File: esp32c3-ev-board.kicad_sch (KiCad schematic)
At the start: 23 parts, among them IC1 ESP32-C3, IC3 ACS711EEXTK-31AB-T, J1 Battery Neg(Series), J2 Battery Pos

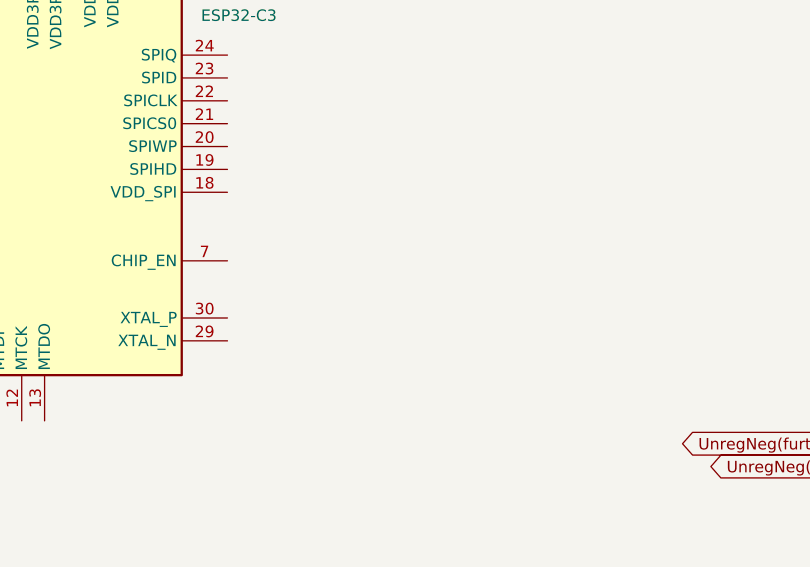
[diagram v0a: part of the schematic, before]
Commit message: Crystal added
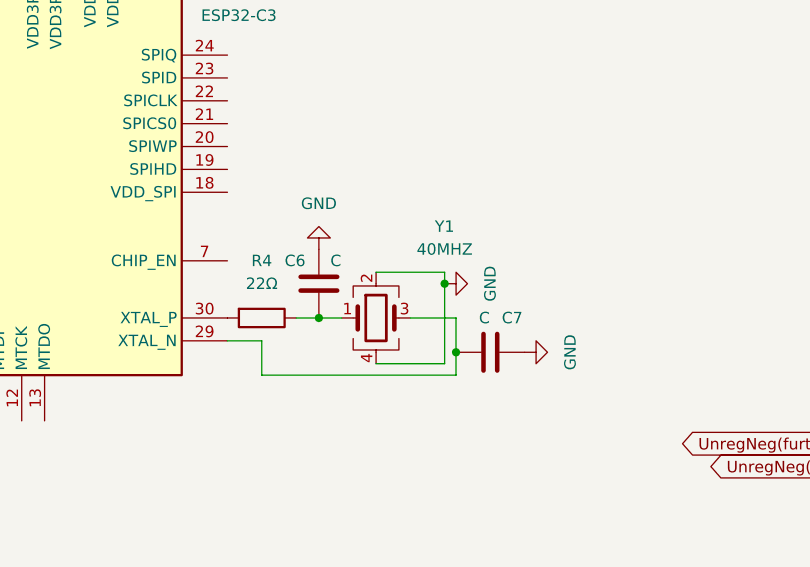
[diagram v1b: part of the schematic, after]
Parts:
- added C6, C7: C, symbol Device:C
- added R4: 22Ω, symbol Device:R
- added Y1: 40MHZ, symbol Device:Crystal_GND24
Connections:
- net GND: now also C6.2, C7.2, Y1.2, Y1.4
- net at IC1.29 (XTAL_N): now also C7.1, Y1.3
- net at IC1.30 (XTAL_P): now also R4.2
- new net: C6.1, R4.1, Y1.1
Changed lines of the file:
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@@
   (junction (at 33.02 69.85) (diameter 0) (color 0 0 0 0)
   )
+  (junction (at 116.84 101.6) (diameter 0) (color 0 0 0 0)
+  )
   (junction (at 77.47 54.61) (diameter 0) (color 0 0 0 0)
   )
@@
   )
   (junction (at 116.84 45.72) (diameter 0) (color 0 0 0 0)
+  )
+  (junction (at 130.81 97.79) (diameter 0) (color 0 0 0 0)
+  )
+  (junction (at 132.08 105.41) (diameter 0) (color 0 0 0 0)
   )
   (junction (at 60.96 29.21) (diameter 0) (color 0 0 0 0)
@@
     (stroke (width 0) (type default))
   )
+  (wire (pts (xy 132.08 105.41) (xy 132.08 107.95))
+    (stroke (width 0) (type default))
+  )
+  (wire (pts (xy 110.49 104.14) (xy 106.68 104.14))
+    (stroke (width 0) (type default))
+  )
   (wire (pts (xy 91.44 38.1) (xy 91.44 54.61))
     (stroke (width 0) (type default))
@@
     (stroke (width 0) (type default))
   )
+  (wire (pts (xy 132.08 101.6) (xy 132.08 105.41))
+    (stroke (width 0) (type default))
+  )
+  (wire (pts (xy 130.81 106.68) (xy 123.19 106.68))
+    (stroke (width 0) (type default))
+  )
+  (wire (pts (xy 130.81 97.79) (xy 130.81 106.68))
+    (stroke (width 0) (type default))
+  )
   (wire (pts (xy 103.505 38.1) (xy 97.155 38.1))
     (stroke (width 0) (type default))
@@
     (stroke (width 0) (type default))
   )
+  (wire (pts (xy 116.84 101.6) (xy 114.3 101.6))
+    (stroke (width 0) (type default))
+  )
   (wire (pts (xy 201.93 95.25) (xy 201.93 100.33))
     (stroke (width 0) (type default))
@@
     (stroke (width 0) (type default))
   )
+  (wire (pts (xy 127 101.6) (xy 132.08 101.6))
+    (stroke (width 0) (type default))
+  )
+  (wire (pts (xy 119.38 101.6) (xy 116.84 101.6))
+    (stroke (width 0) (type default))
+  )
   (wire (pts (xy 29.21 73.66) (xy 29.21 77.47))
     (stroke (width 0) (type default))
@@
     (stroke (width 0) (type default))
   )
+  (wire (pts (xy 123.19 96.52) (xy 130.81 96.52))
+    (stroke (width 0) (type default))
+  )
   (wire (pts (xy 189.23 132.08) (xy 189.23 135.89))
     (stroke (width 0) (type default))
@@
     (stroke (width 0) (type default))
   )
+  (wire (pts (xy 110.49 107.95) (xy 110.49 104.14))
+    (stroke (width 0) (type default))
+  )
+  (wire (pts (xy 130.81 96.52) (xy 130.81 97.79))
+    (stroke (width 0) (type default))
+  )
   (wire (pts (xy 48.26 69.85) (xy 60.96 69.85))
+    (stroke (width 0) (type default))
+  )
+  (wire (pts (xy 132.08 107.95) (xy 110.49 107.95))
     (stroke (width 0) (type default))
   )
@@
     )
   )
+  (symbol (lib_id "Device:Crystal_GND24") (at 123.19 101.6 0) (unit 1)
+    (in_bom yes) (on_board yes) (dnp no)
+    (property "Reference" "Y1" (at 130.81 91.44 0)
+      (effects (font (size 1.27 1.27)))
+    )
+    (property "Value" "40MHZ" (at 130.81 93.98 0)
+      (effects (font (size 1.27 1.27)))
+    )
+    (property "Footprint" "" (at 123.19 101.6 0)
+      (effects (font (size 1.27 1.27)) hide)
+    )
+    (property "Datasheet" "~" (at 123.19 101.6 0)
+      (effects (font (size 1.27 1.27)) hide)
+    )
+    (pin "1")
+    (pin "2")
+    (pin "3")
+    (pin "4")
+    (instances
+      (project "esp32c3-ev-board"
+        (path "/f5da1fcc-93b5-4c63-bb34-c18c11bc243c"
+          (reference "Y1") (unit 1)
+        )
+      )
+    )
+  )
   (symbol (lib_id "Device:D") (at 189.23 139.7 90) (unit 1)
     (in_bom yes) (on_board yes) (dnp no) (fields_autoplaced)
@@
         (path "/f5da1fcc-93b5-4c63-bb34-c18c11bc243c"
           (reference "#PWR04") (unit 1)
+        )
+      )
+    )
+  )
+  (symbol (lib_id "power:GND") (at 139.7 105.41 90) (unit 1)
+    (in_bom yes) (on_board yes) (dnp no) (fields_autoplaced)
+    (property "Reference" "#PWR09" (at 146.05 105.41 0)
+      (effects (font (size 1.27 1.27)) hide)
+    )
+    (property "Value" "GND" (at 144.78 105.41 0)
+      (effects (font (size 1.27 1.27)))
+    )
+    (property "Footprint" "" (at 139.7 105.41 0)
+      (effects (font (size 1.27 1.27)) hide)
+    )
+    (property "Datasheet" "" (at 139.7 105.41 0)
+      (effects (font (size 1.27 1.27)) hide)
+    )
+    (pin "1")
+    (instances
+      (project "esp32c3-ev-board"
+        (path "/f5da1fcc-93b5-4c63-bb34-c18c11bc243c"
+          (reference "#PWR09") (unit 1)
         )
       )
@@
     )
   )
+  (symbol (lib_id "Device:C") (at 135.89 105.41 90) (unit 1)
+    (in_bom yes) (on_board yes) (dnp no)
+    (property "Reference" "C7" (at 137.16 101.6 90)
+      (effects (font (size 1.27 1.27)) (justify right))
+    )
+    (property "Value" "C" (at 134.62 101.6 90)
+      (effects (font (size 1.27 1.27)) (justify right))
+    )
+    (property "Footprint" "" (at 139.7 104.4448 0)
+      (effects (font (size 1.27 1.27)) hide)
+    )
+    (property "Datasheet" "~" (at 135.89 105.41 0)
+      (effects (font (size 1.27 1.27)) hide)
+    )
+    (pin "1")
+    (pin "2")
+    (instances
+      (project "esp32c3-ev-board"
+        (path "/f5da1fcc-93b5-4c63-bb34-c18c11bc243c"
+          (reference "C7") (unit 1)
+        )
+      )
+    )
+  )
   (symbol (lib_id "Connector:Screw_Terminal_01x01") (at 137.16 182.88 270) (unit 1)
     (in_bom yes) (on_board yes) (dnp no)
@@
     )
   )
+  (symbol (lib_id "Device:C") (at 116.84 97.79 180) (unit 1)
+    (in_bom yes) (on_board yes) (dnp no)
+    (property "Reference" "C6" (at 113.03 95.25 0)
+      (effects (font (size 1.27 1.27)) (justify right))
+    )
+    (property "Value" "C" (at 118.11 95.25 0)
+      (effects (font (size 1.27 1.27)) (justify right))
+    )
+    (property "Footprint" "" (at 115.8748 93.98 0)
+      (effects (font (size 1.27 1.27)) hide)
+    )
+    (property "Datasheet" "~" (at 116.84 97.79 0)
+      (effects (font (size 1.27 1.27)) hide)
+    )
+    (pin "1")
+    (pin "2")
+    (instances
+      (project "esp32c3-ev-board"
+        (path "/f5da1fcc-93b5-4c63-bb34-c18c11bc243c"
+          (reference "C6") (unit 1)
+        )
+      )
+    )
+  )
+  (symbol (lib_id "power:GND") (at 116.84 93.98 180) (unit 1)
+    (in_bom yes) (on_board yes) (dnp no) (fields_autoplaced)
+    (property "Reference" "#PWR08" (at 116.84 87.63 0)
+      (effects (font (size 1.27 1.27)) hide)
+    )
+    (property "Value" "GND" (at 116.84 88.9 0)
+      (effects (font (size 1.27 1.27)))
+    )
+    (property "Footprint" "" (at 116.84 93.98 0)
+      (effects (font (size 1.27 1.27)) hide)
+    )
+    (property "Datasheet" "" (at 116.84 93.98 0)
+      (effects (font (size 1.27 1.27)) hide)
+    )
+    (pin "1")
+    (instances
+      (project "esp32c3-ev-board"
+        (path "/f5da1fcc-93b5-4c63-bb34-c18c11bc243c"
+          (reference "#PWR08") (unit 1)
+        )
+      )
+    )
+  )
   (symbol (lib_id "Device:C") (at 193.04 135.89 90) (unit 1)
     (in_bom yes) (on_board yes) (dnp no)
@@
         )
       )
+    )
+  )
+  (symbol (lib_id "Device:R") (at 110.49 101.6 270) (unit 1)
+    (in_bom yes) (on_board yes) (dnp no) (fields_autoplaced)
+    (property "Reference" "R4" (at 110.49 95.25 90)
+      (effects (font (size 1.27 1.27)))
+    )
+    (property "Value" "22Ω" (at 110.49 97.79 90)
+      (effects (font (size 1.27 1.27)))
+    )
+    (property "Footprint" "" (at 110.49 99.822 90)
+      (effects (font (size 1.27 1.27)) hide)
+    )
+    (property "Datasheet" "~" (at 110.49 101.6 0)
+      (effects (font (size 1.27 1.27)) hide)
+    )
+    (pin "1")
+    (pin "2")
+    (instances
+      (project "esp32c3-ev-board"
+        (path "/f5da1fcc-93b5-4c63-bb34-c18c11bc243c"
+          (reference "R4") (unit 1)
+        )
+      )
+    )
+  )
+  (symbol (lib_id "power:GND") (at 130.81 97.79 90) (unit 1)
+    (in_bom yes) (on_board yes) (dnp no) (fields_autoplaced)
+    (property "Reference" "#PWR010" (at 137.16 97.79 0)
+      (effects (font (size 1.27 1.27)) hide)
+    )
+    (property "Value" "GND" (at 135.89 97.79 0)
+      (effects (font (size 1.27 1.27)))
+    )
+    (property "Footprint" "" (at 130.81 97.79 0)
+      (effects (font (size 1.27 1.27)) hide)
+    )
+    (property "Datasheet" "" (at 130.81 97.79 0)
+      (effects (font (size 1.27 1.27)) hide)
+    )
+    (pin "1")
+    (instances
+      (project "esp32c3-ev-board"
+        (path "/f5da1fcc-93b5-4c63-bb34-c18c11bc243c"
+          (reference "#PWR010") (unit 1)
+        )
+      )

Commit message: rando resistor test
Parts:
- added R5: 22Ω, symbol Device:R
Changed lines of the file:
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@@
+    )
+  )
+  (symbol (lib_id "Device:R") (at 132.08 83.82 270) (unit 1)
+    (in_bom yes) (on_board yes) (dnp no) (fields_autoplaced)
+    (property "Reference" "R5" (at 132.08 77.47 90)
+      (effects (font (size 1.27 1.27)))
+    )
+    (property "Value" "22Ω" (at 132.08 80.01 90)
+      (effects (font (size 1.27 1.27)))
+    )
+    (property "Footprint" "" (at 132.08 82.042 90)
+      (effects (font (size 1.27 1.27)) hide)
+    )
+    (property "Datasheet" "~" (at 132.08 83.82 0)
+      (effects (font (size 1.27 1.27)) hide)
+    )
+    (pin "1")
+    (pin "2")
+    (instances
+      (project "esp32c3-ev-board"
+        (path "/f5da1fcc-93b5-4c63-bb34-c18c11bc243c"
+          (reference "R5") (unit 1)
+        )
+      )
     )
   )

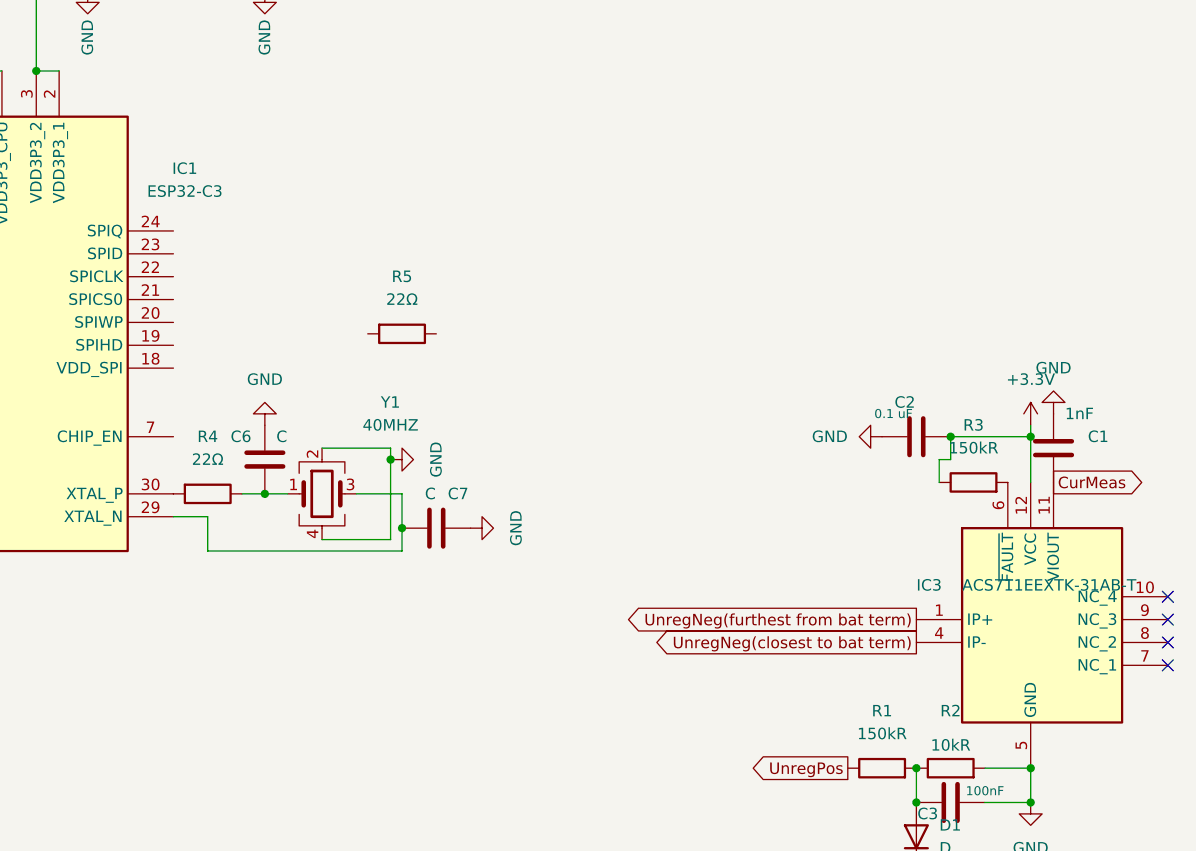
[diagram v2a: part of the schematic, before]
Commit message: Flash Memory Added
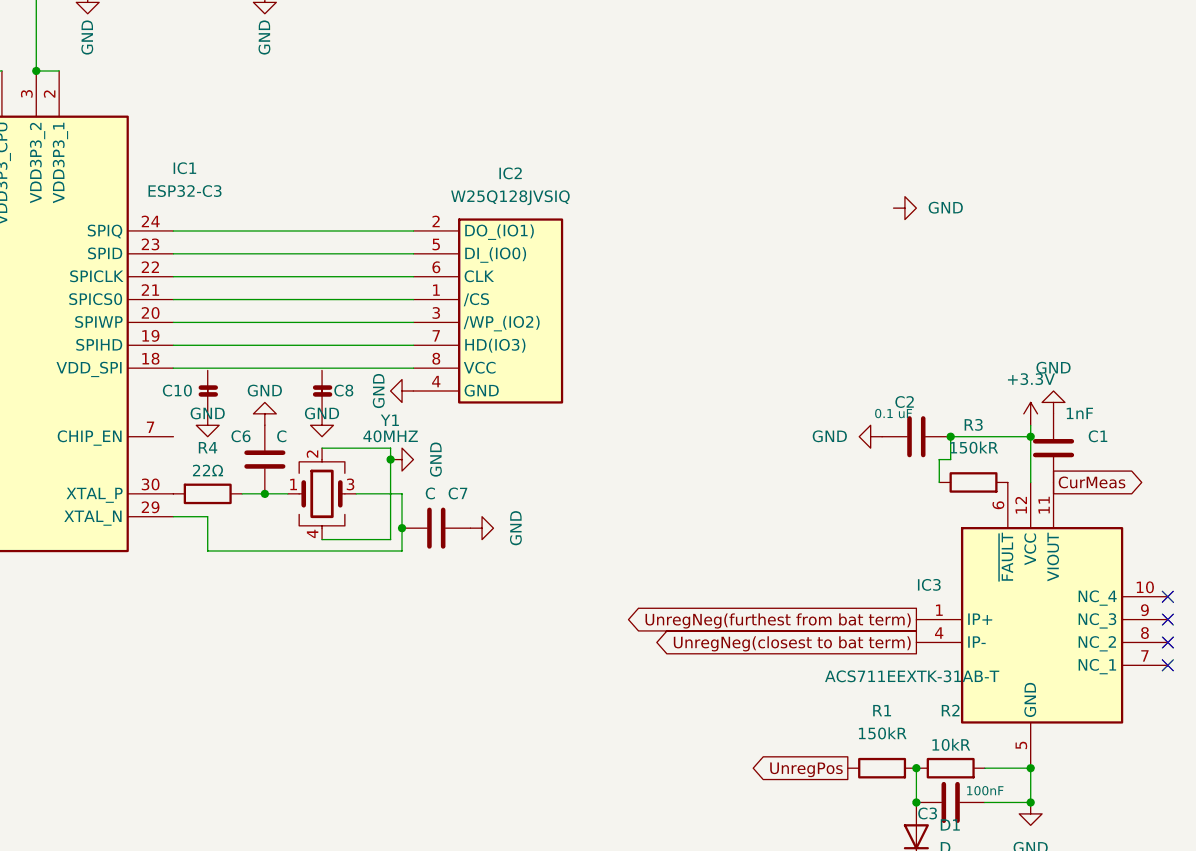
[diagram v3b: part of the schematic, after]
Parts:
- removed R5: 22Ω, symbol Device:R
- added C10, C8: C, symbol Device:C
- added IC2: W25Q128JVSIQ, SOIC127P790X216-8N, symbol W25Q128JVSIQ:W25Q128JVSIQ
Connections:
- net GND: now also C10.2, C8.2, IC2.4 (GND)
- net at IC1.18 (VDD_SPI): now also IC2.8 (VCC)
- net at IC1.19 (SPIHD): now also IC2.7 (HD(IO3))
- net at IC1.20 (SPIWP): now also IC2.3 (/WP_(IO2))
- net at IC1.21 (SPICS0): now also IC2.1 (/CS)
- net at IC1.22 (SPICLK): now also IC2.6 (CLK)
- net at IC1.23 (SPID): now also IC2.5 (DI_(IO0))
- net at IC1.24 (SPIQ): now also IC2.2 (DO_(IO1))

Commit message: Cleaning up Schematic
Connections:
- net at IC1.18 (VDD_SPI), IC2.8 (VCC): now also C10.1, C8.1

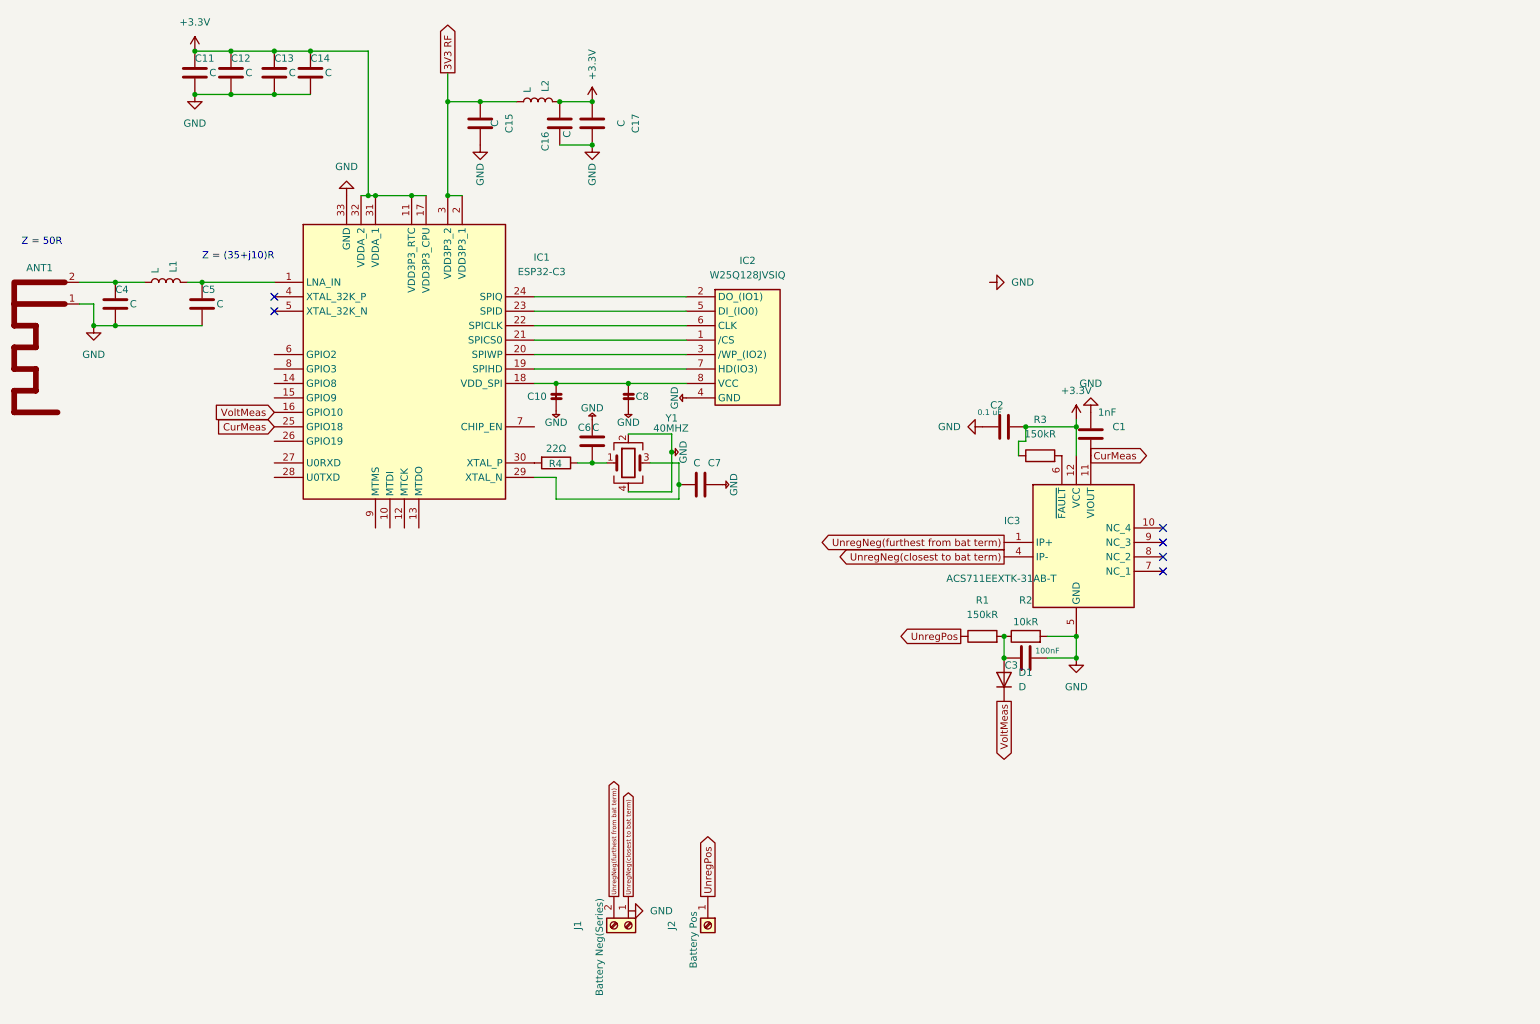
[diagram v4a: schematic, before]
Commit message: Added Chip Enable Switch
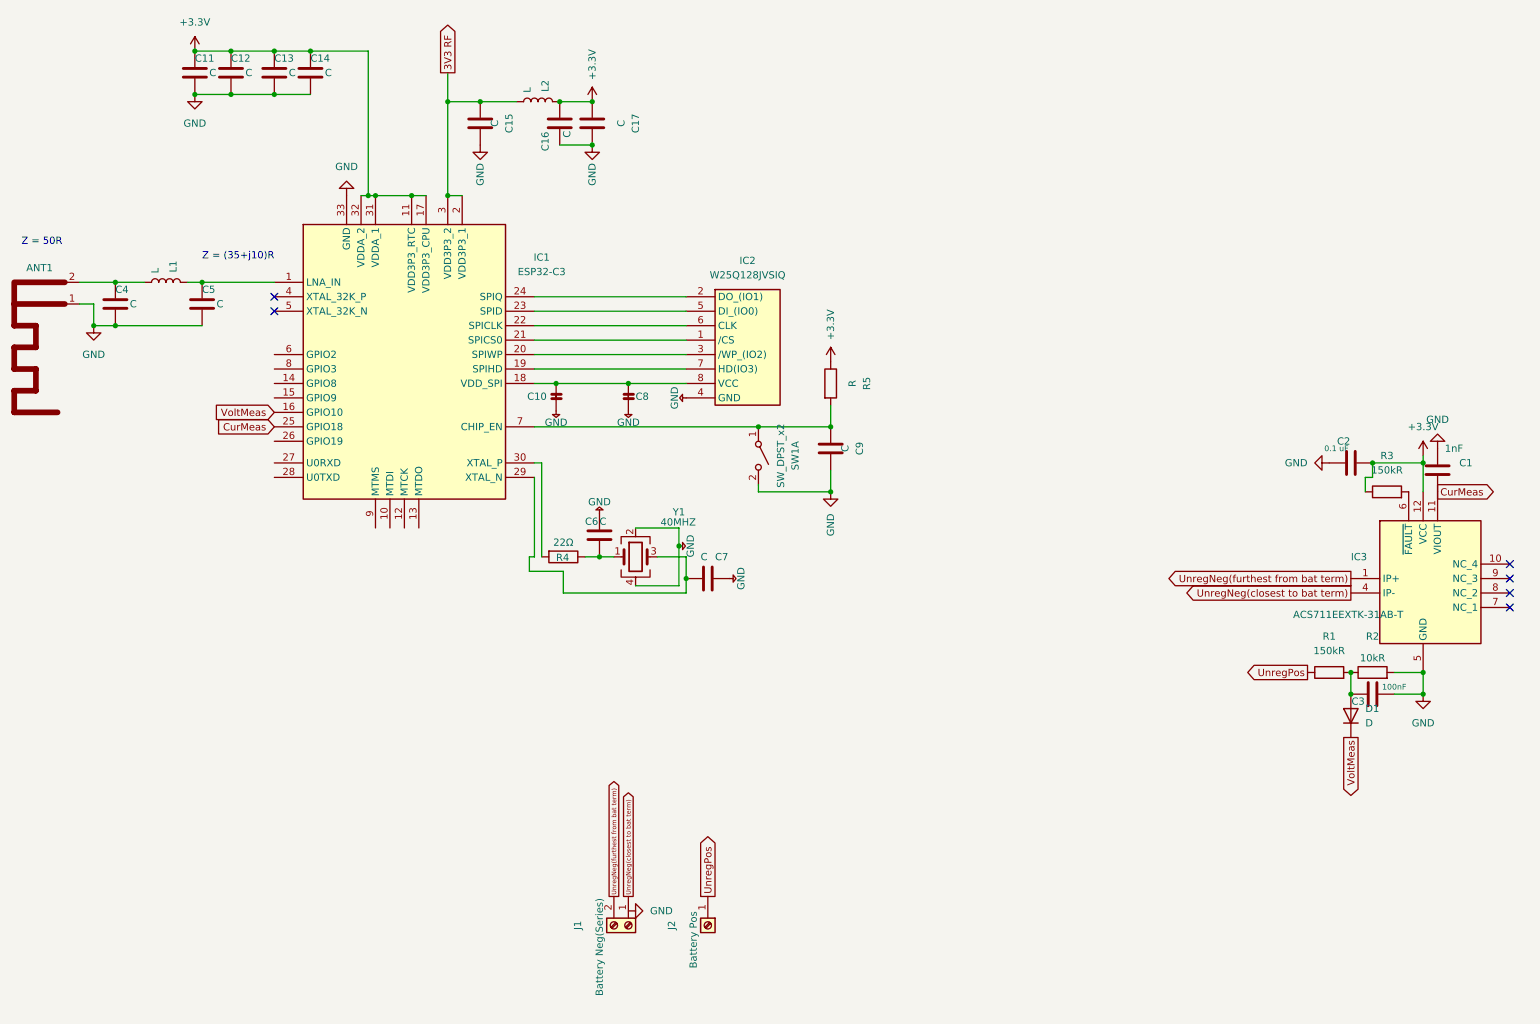
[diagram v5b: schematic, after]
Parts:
- added C9: C, symbol Device:C
- added R5: R, symbol Device:R
- added SW1: SW_DPST_x2, symbol Switch:SW_DPST_x2
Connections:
- net +3.3V: now also R5.1
- net GND: now also C9.2, SW1.2 (B)
- net at IC1.7 (CHIP_EN): now also C9.1, R5.2, SW1.1 (A)
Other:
- moved on the sheet: C1, C2, C3, C6, C7, D1, IC3, R1, R2, R3, R4, Y1
